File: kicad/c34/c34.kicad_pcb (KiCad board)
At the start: 2 copper layers, 35.6 x 51.4 mm, 20 parts, among them K1 SANYOU_SRD_Form_C, Q1 TRANS_NPN-MMBT2222AL, SW1 SW_Push, U1 MOUDLE-SEEEDUINO-XIAO-ESP32C3

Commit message: v1.2.0
maj kicad
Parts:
- removed the G*** at (124.4, 72.7)
- removed the G*** at (127.9, 106.3)
- added G***: LOGO, logo_fb:fbs, F.Cu at (124.6, 74.9)
- added G***: LOGO, logo_fb:fbs, B.Cu at (127.9, 106.3)
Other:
- board text added: "FBS V1.00"
- board text removed: "FuméeBleue V1.00"

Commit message: Update c34.kicad_pcb
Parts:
- R2: value 10k -> 1k
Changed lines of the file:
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@@
 			)
 		)
-		(property "Footprint" ""
+		(property "Footprint" "TerminalBlock:TerminalBlock_Altech_AK300-3_P5.00mm"
 			(at 0 0 180)
 			(unlocked yes)
@@
 			)
 		)
-		(property "Description" "Generic screw terminal, single row, 01x03, script generated (kicad-library-utils/schlib/autogen/connector/)"
+		(property "Description" ""
 			(at 0 0 180)
 			(unlocked yes)
@@
 			)
 		)
+		(property ki_fp_filters "TerminalBlock*:*")
+		(sheetname "Racine")
 		(sheetfile "c34.kicad_sch")
 		(attr through_hole)
@@
 			)
 		)
-		(property "Footprint" ""
+		(property "Footprint" "LED_SMD:LED_Inolux_IN-PI554FCH_PLCC4_5.0x5.0mm_P3.2mm"
 			(at 0 0 0)
 			(unlocked yes)
@@
 			)
 		)
-		(property "Datasheet" ""
+		(property "Datasheet" "http://www.inolux-corp.com/datasheet/SMDLED/Addressable%20LED/IN-PI554FCH.pdf"
 			(at 0 0 0)
 			(unlocked yes)
@@
 			)
 		)
-		(property "Description" "5050 RGB LED 4-Pin with integrated IC"
+		(property "Description" ""
 			(at 0 0 0)
 			(unlocked yes)
@@
 			)
 		)
+		(property ki_fp_filters "LED*IN-PI554FCH*PLCC*5.0x5.0mm*P3.2mm*")
+		(sheetname "Racine")
 		(sheetfile "c34.kicad_sch")
 		(attr smd)
@@
 			)
 		)
-		(property "Footprint" ""
+		(property "Footprint" "LED_SMD:LED_Inolux_IN-PI554FCH_PLCC4_5.0x5.0mm_P3.2mm"
 			(at 0 0 0)
 			(unlocked yes)
@@
 			)
 		)
-		(property "Datasheet" ""
+		(property "Datasheet" "http://www.inolux-corp.com/datasheet/SMDLED/Addressable%20LED/IN-PI554FCH.pdf"
 			(at 0 0 0)
 			(unlocked yes)
@@
 			)
 		)
-		(property "Description" "5050 RGB LED 4-Pin with integrated IC"
+		(property "Description" ""
 			(at 0 0 0)
 			(unlocked yes)
@@
 			)
 		)
+		(property ki_fp_filters "LED*IN-PI554FCH*PLCC*5.0x5.0mm*P3.2mm*")
+		(sheetname "Racine")
 		(sheetfile "c34.kicad_sch")
 		(attr smd)
@@
 			)
 		)
-		(property "Footprint" ""
+		(property "Footprint" "Fuseholder 696310001002:696310001002"
 			(at 0 0 90)
 			(unlocked yes)
@@
 			)
 		)
-		(property "Description" "Fuse"
+		(property "Description" ""
 			(at 0 0 90)
 			(unlocked yes)
@@
 			)
 		)
+		(property ki_fp_filters "*Fuse*")
+		(sheetname "Racine")
 		(sheetfile "c34.kicad_sch")
 		(attr through_hole)
@@
 			)
 		)
-		(property "Footprint" ""
+		(property "Footprint" "Relay_THT:Relay_SPDT_SANYOU_SRD_Series_Form_C"
 			(at 0 0 0)
 			(unlocked yes)
@@
 			)
 		)
-		(property "Datasheet" ""
+		(property "Datasheet" "http://www.sanyourelay.ca/public/products/pdf/SRD.pdf"
 			(at 0 0 0)
 			(unlocked yes)
@@
 			)
 		)
-		(property "Description" "Sanyo SRD relay, Single Pole Miniature Power Relay,"
+		(property "Description" ""
 			(at 0 0 0)
 			(unlocked yes)
@@
 			)
 		)
+		(property ki_fp_filters "Relay*SPDT*SANYOU*SRD*Series*Form*C*")
+		(sheetname "Racine")
 		(sheetfile "c34.kicad_sch")
 		(attr through_hole)
@@
 			)
 		)
-		(property "Footprint" ""
+		(property "Footprint" "LED_SMD:LED_Inolux_IN-PI554FCH_PLCC4_5.0x5.0mm_P3.2mm"
 			(at 0 0 0)
 			(unlocked yes)
@@
 			)
 		)
-		(property "Datasheet" ""
+		(property "Datasheet" "http://www.inolux-corp.com/datasheet/SMDLED/Addressable%20LED/IN-PI554FCH.pdf"
 			(at 0 0 0)
 			(unlocked yes)
@@
 			)
 		)
-		(property "Description" "5050 RGB LED 4-Pin with integrated IC"
+		(property "Description" ""
 			(at 0 0 0)
 			(unlocked yes)
@@
 			)
 		)
+		(property ki_fp_filters "LED*IN-PI554FCH*PLCC*5.0x5.0mm*P3.2mm*")
+		(sheetname "Racine")
 		(sheetfile "c34.kicad_sch")
 		(attr smd)
@@
 			)
 		)
-		(property "Footprint" ""
+		(property "Footprint" "LED_SMD:LED_Inolux_IN-PI554FCH_PLCC4_5.0x5.0mm_P3.2mm"
 			(at 0 0 0)
 			(unlocked yes)
@@
 			)
 		)
-		(property "Datasheet" ""
+		(property "Datasheet" "http://www.inolux-corp.com/datasheet/SMDLED/Addressable%20LED/IN-PI554FCH.pdf"
 			(at 0 0 0)
 			(unlocked yes)
@@
 			)
 		)
-		(property "Description" "5050 RGB LED 4-Pin with integrated IC"
+		(property "Description" ""
 			(at 0 0 0)
 			(unlocked yes)
@@
 			)
 		)
+		(property ki_fp_filters "LED*IN-PI554FCH*PLCC*5.0x5.0mm*P3.2mm*")
+		(sheetname "Racine")
 		(sheetfile "c34.kicad_sch")
 		(attr smd)
@@
 			)
 		)
-		(property "Footprint" ""
+		(property "Footprint" "Button_Switch_SMD:SW_SPST_CK_RS282G05A3"
 			(at 0 0 90)
 			(unlocked yes)
@@
 			)
 		)
-		(property "Description" "Push button switch, generic, two pins"
+		(property "Description" ""
 			(at 0 0 90)
 			(unlocked yes)
@@
 			)
 		)
+		(sheetname "Racine")
 		(sheetfile "c34.kicad_sch")
 		(attr smd)
@@
 			)
 		)
-		(property "Footprint" ""
+		(property "Footprint" "Package_TO_SOT_SMD:SOT-23"
 			(at 0 0 -90)
 			(unlocked yes)
@@
 			)
 		)
-		(property "Description" "NPN transistor Current controlled devices typically used to amplify current or used as a switch. <ul>  <li>    BC547 -     <a href=\"http://www.sparkfun.com/products/8928\">COM-08928</a>    (TO-92 45V 100mA) (1.Collector 2.Base 3.Emitter)  </li>  <li>    2N3904 -     <a href=\"http://www.sparkfun.com/products/521\">COM-00521</a>    (TO-92 40V 200mA) (1.Emitter 2.Base 3.Collector)  </li>  <li>    P2N2222A -     <a href=\"http://www.sparkfun.com/products/12852\">COM-12852</a>    (TO-92 40V 600mA) (1.Collector 2.Base 3.Emitter)  </li></ul>"
+		(property "Description" ""
 			(at 0 0 -90)
 			(unlocked yes)
@@
 			)
 		)
+		(property ki_fp_filters "*SOT23-3* *SOT23-3*")
+		(sheetname "Racine")
 		(sheetfile "c34.kicad_sch")
 		(attr smd)
@@
 			)
 		)
-		(property "Footprint" ""
+		(property "Footprint" "Capacitor_SMD:C_1210_3225Metric_Pad1.33x2.70mm_HandSolder"
 			(at 0 0 -90)
 			(unlocked yes)
@@
 			)
 		)
-		(property "Description" "Polarized capacitor"
+		(property "Description" ""
 			(at 0 0 -90)
 			(unlocked yes)
@@
 			)
 		)
+		(property ki_fp_filters "CP_*")
+		(sheetname "Racine")
 		(sheetfile "c34.kicad_sch")
 		(attr smd)
@@
 			)
 		)
-		(property "Footprint" ""
+		(property "Footprint" "Diode_SMD:D_MiniMELF"
 			(at 0 0 90)
 			(unlocked yes)
@@
 			)
 		)
-		(property "Datasheet" ""
+		(property "Datasheet" "http://www.vishay.com/docs/85557/ll4148.pdf"
 			(at 0 0 90)
 			(unlocked yes)
@@
 			)
 		)
-		(property "Description" "100V 0.15A standard switching diode, MiniMELF"
+		(property "Description" ""
 			(at 0 0 90)
 			(unlocked yes)
@@
 			)
 		)
+		(property ki_fp_filters "D*MiniMELF*")
+		(sheetname "Racine")
 		(sheetfile "c34.kicad_sch")
 		(attr smd)
@@
 			)
 		)
-		(property "Footprint" ""
+		(property "Footprint" "Resistor_SMD:R_1206_3216Metric_Pad1.30x1.75mm_HandSolder"
 			(at 0 0 90)
 			(unlocked yes)
@@
 			)
 		)
-		(property "Description" "Resistor"
+		(property "Description" ""
 			(at 0 0 90)
 			(unlocked yes)
@@
 			)
 		)
+		(property ki_fp_filters "R_*")
+		(sheetname "Racine")
 		(sheetfile "c34.kicad_sch")
 		(attr smd)
@@
 			)
 		)
-		(property "Footprint" ""
+		(property "Footprint" "esp32c3:MOUDLE14P-SMD-2.54-21X17.8MM"
 			(at 0 0 180)
 			(unlocked yes)
@@
 			)
 		)
+		(sheetname "Racine")
 		(sheetfile "c34.kicad_sch")
 		(attr through_hole)
@@
 			)
 		)
-		(property "Value" "10k"
+		(property "Value" "1k"
 			(at 0 -1.82 90)
 			(layer "B.Fab")
@@
 			)
 		)
-		(property "Footprint" ""
+		(property "Footprint" "Resistor_SMD:R_1206_3216Metric_Pad1.30x1.75mm_HandSolder"
 			(at 0 0 90)
 			(unlocked yes)
@@
 			)
 		)
-		(property "Description" "Resistor"
+		(property "Description" ""
 			(at 0 0 90)
 			(unlocked yes)
@@
 			)
 		)
+		(property ki_fp_filters "R_*")
+		(sheetname "Racine")
 		(sheetfile "c34.kicad_sch")
 		(attr smd)

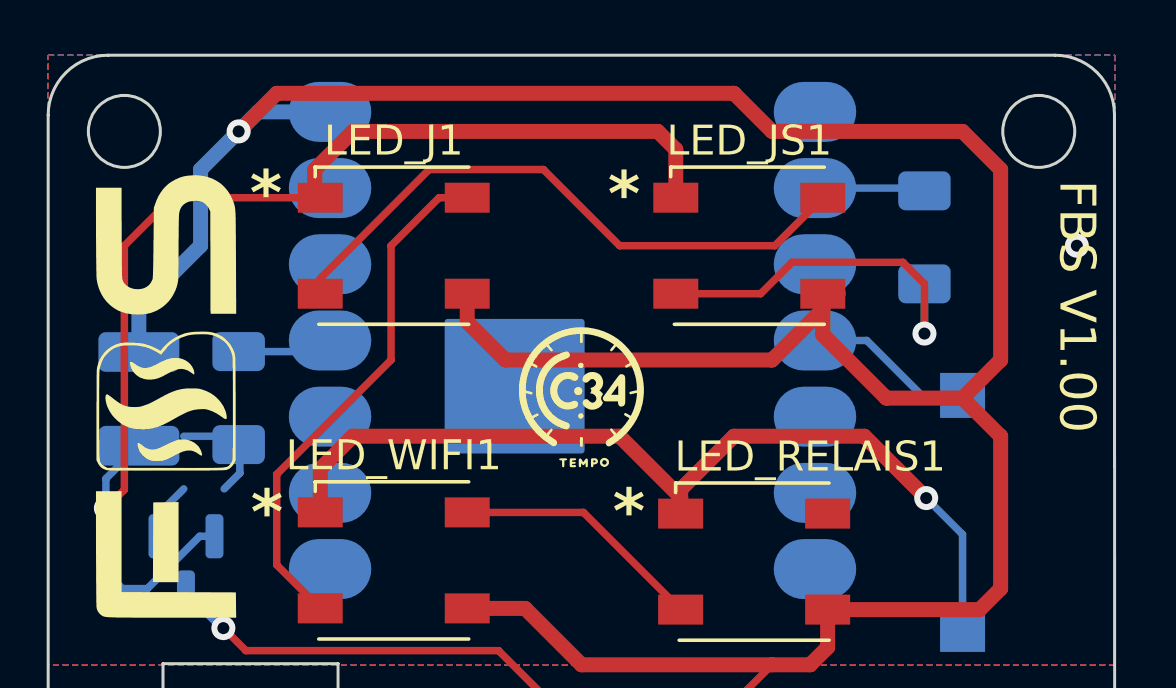
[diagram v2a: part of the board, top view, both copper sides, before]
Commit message: v1.3.1
Intégration pages web en zone PROGMEM et modif pcb 1.1
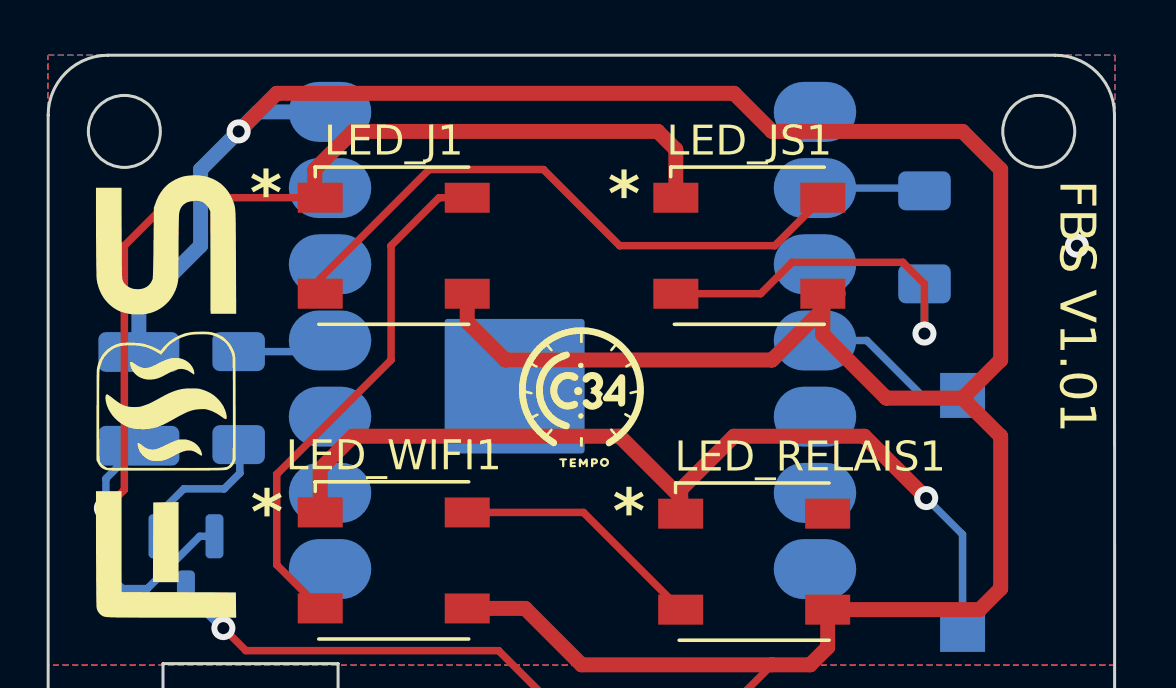
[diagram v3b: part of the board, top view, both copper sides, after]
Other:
- board text added: "FBS V1.01"
- board text removed: "FBS V1.00"
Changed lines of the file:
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@@
 				(font
 					(size 1.27 1.27)
+					(thickness 0.15)
 				)
 			)
@@
 				(font
 					(size 1.27 1.27)
+					(thickness 0.15)
 				)
 			)
@@
 				(font
 					(size 1.27 1.27)
+					(thickness 0.15)
 				)
 			)
@@
 				(font
 					(size 1.27 1.27)
+					(thickness 0.15)
 				)
 			)
@@
 				(font
 					(size 1.27 1.27)
+					(thickness 0.15)
 				)
 			)
@@
 				(font
 					(size 1.27 1.27)
+					(thickness 0.15)
 				)
 			)
@@
 				(font
 					(size 1.27 1.27)
+					(thickness 0.15)
 				)
 			)
@@
 				(font
 					(size 1.27 1.27)
+					(thickness 0.15)
 				)
 			)
@@
 				(font
 					(size 1.27 1.27)
+					(thickness 0.15)
 				)
 			)
@@
 				(font
 					(size 1.27 1.27)
+					(thickness 0.15)
 				)
 			)
@@
 				(font
 					(size 1.27 1.27)
+					(thickness 0.15)
 				)
 			)
@@
 				(font
 					(size 1.27 1.27)
+					(thickness 0.15)
 				)
 			)
@@
 				(font
 					(size 1.27 1.27)
+					(thickness 0.15)
 				)
 			)
@@
 				(font
 					(size 1.27 1.27)
+					(thickness 0.15)
 				)
 			)
@@
 				(font
 					(size 1.27 1.27)
+					(thickness 0.15)
 				)
 			)
@@
 				(font
 					(size 1.27 1.27)
+					(thickness 0.15)
 				)
 			)
@@
 				(font
 					(size 1.27 1.27)
+					(thickness 0.15)
 				)
 			)
@@
 				(font
 					(size 1.27 1.27)
+					(thickness 0.15)
 				)
 			)
@@
 				(font
 					(size 1.27 1.27)
+					(thickness 0.15)
 				)
 			)
@@
 				(font
 					(size 1.27 1.27)
+					(thickness 0.15)
 				)
 			)
@@
 				(font
 					(size 1.27 1.27)
+					(thickness 0.15)
 				)
 			)
@@
 				(font
 					(size 1.27 1.27)
+					(thickness 0.15)
 				)
 			)
@@
 				(font
 					(size 1.27 1.27)
+					(thickness 0.15)
 				)
 			)
@@
 				(font
 					(size 1.27 1.27)
+					(thickness 0.15)
 				)
 			)
@@
 				(font
 					(size 1.27 1.27)
+					(thickness 0.15)
 				)
 			)
@@
 				(font
 					(size 1.27 1.27)
+					(thickness 0.15)
 				)
 			)
@@
 				(font
 					(size 1.27 1.27)
+					(thickness 0.15)
 				)
 			)
@@
 				(font
 					(size 1.27 1.27)
+					(thickness 0.15)
 				)
 			)
@@
 				(font
 					(size 1.27 1.27)
+					(thickness 0.15)
 				)
 			)
@@
 				(font
 					(size 1.27 1.27)
+					(thickness 0.15)
 				)
 			)
@@
 				(font
 					(size 1.27 1.27)
+					(thickness 0.15)
 				)
 			)
@@
 				(font
 					(size 1.27 1.27)
+					(thickness 0.15)
 				)
 			)
@@
 				(font
 					(size 1.27 1.27)
+					(thickness 0.15)
 				)
 			)
@@
 				(font
 					(size 1.27 1.27)
+					(thickness 0.15)
 				)
 			)
@@
 				(font
 					(size 1.27 1.27)
+					(thickness 0.15)
 				)
 			)
@@
 				(font
 					(size 1.27 1.27)
+					(thickness 0.15)
 				)
 			)
@@
 				(font
 					(size 1.27 1.27)
+					(thickness 0.15)
 				)
 			)
@@
 				(font
 					(size 1.27 1.27)
+					(thickness 0.15)
 				)
 			)
@@
 				(font
 					(size 1.27 1.27)
+					(thickness 0.15)
 				)
 			)
@@
 				(font
 					(size 1.27 1.27)
+					(thickness 0.15)
 				)
 			)
@@
 				(font
 					(size 1.27 1.27)
+					(thickness 0.15)
 				)
 			)
@@
 				(font
 					(size 1.27 1.27)
+					(thickness 0.15)
 				)
 			)
@@
 				(font
 					(size 1.27 1.27)
+					(thickness 0.15)
 				)
 			)
@@
 				(font
 					(size 1.27 1.27)
+					(thickness 0.15)
 				)
 			)
@@
 				(font
 					(size 1.27 1.27)
+					(thickness 0.15)
 				)
 			)
@@
 				(font
 					(size 1.27 1.27)
+					(thickness 0.15)
 				)
 			)
@@
 				(font
 					(size 1.27 1.27)
+					(thickness 0.15)
 				)
 			)
@@
 				(font
 					(size 1.27 1.27)
+					(thickness 0.15)
 				)
 			)
@@
 				(font
 					(size 1.27 1.27)
+					(thickness 0.15)
 				)
 			)
@@
 				(font
 					(size 1.27 1.27)
+					(thickness 0.15)
 				)
 			)
@@
 				(font
 					(size 1.27 1.27)
+					(thickness 0.15)
 				)
 			)
@@
 				(font
 					(size 1.27 1.27)
+					(thickness 0.15)
 				)
 			)
@@
 				(font
 					(size 1.27 1.27)
+					(thickness 0.15)
 				)
 			)
@@
 				(font
 					(size 1.27 1.27)
+					(thickness 0.15)
 				)
 			)
@@
 				(font
 					(size 1.27 1.27)
+					(thickness 0.15)
 				)
 			)
@@
 				(font
 					(size 1.27 1.27)
+					(thickness 0.15)
 				)
 			)
@@
 				(font
 					(size 1.27 1.27)
+					(thickness 0.15)
 				)
 			)
@@
 				(font
 					(size 1.27 1.27)
+					(thickness 0.15)
 				)
 			)
@@
 				(font
 					(size 1.27 1.27)
+					(thickness 0.15)
 				)
 			)
@@
 				(font
 					(size 1.27 1.27)
+					(thickness 0.15)
 				)
 			)
@@
 		)
 	)
-	(gr_text "FBS V1.00"
+	(gr_text "FBS V1.01"
 		(at 154.245286 67.659521 270)
 		(layer "F.SilkS")
@@
 	)
 	(segment
-		(start 126.517312 77.955633)
-		(end 127.040223 77.432722)
+		(start 124.293526 79.535223)
+		(end 124.293526 78.831918)
 		(width 0.25)
 		(layer "B.Cu")
@@
 	)
 	(segment
-		(start 127.040223 77.432722)
-		(end 127.040223 76.520223)
+		(start 124.293526 78.831918)
+		(end 125.169811 77.955633)
 		(width 0.25)
 		(layer "B.Cu")
@@
 	)
 	(segment
-		(start 127.040223 76.520223)
-		(end 127 76.48)
+		(start 125.169811 77.955633)
+		(end 126.517312 77.955633)
 		(width 0.25)
 		(layer "B.Cu")
@@
 	)
 	(segment
-		(start 124.293526 78.831918)
-		(end 125.169811 77.955633)
+		(start 126.517312 77.955633)
+		(end 127.040223 77.432722)
 		(width 0.25)
 		(layer "B.Cu")
@@
 	)
 	(segment
-		(start 124.293526 79.535223)
-		(end 124.293526 78.831918)
+		(start 127.040223 77.432722)
+		(end 127.040223 76.520223)
 		(width 0.25)
 		(layer "B.Cu")
@@
 	)
 	(segment
-		(start 125.169811 76.2)
-		(end 126.517312 76.2)
+		(start 127.040223 76.520223)
+		(end 127 76.48)
 		(width 0.25)
 		(layer "B.Cu")
